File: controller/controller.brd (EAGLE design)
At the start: 100 x 92.7 mm, 26 parts, among them IC1 ATtiny25, IC2 74HC595N

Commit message: Routing erster Versuch
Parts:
- removed JP1: DISABLE, jumper:JP1
- removed R10: (no value), resistor:0617V
- moved SV3 74.0 mm to (76.2, 7.62), turned to 90 degrees
- moved SV2 61.0 mm to (58.4, 7.62), turned to 90 degrees
- moved SV1 51.7 mm to (15.2, 6.35), turned to 0 degrees
- moved R8 41.8 mm to (27.9, 30.5), turned to 0 degrees
- moved R2 39.5 mm to (50.8, 19.1), turned to 270 degrees
- moved R9 37.2 mm to (25.4, 26.7), turned to 0 degrees
- moved LED3 31.4 mm to (55.9, 55.9), turned to 0 degrees
- moved R4 30.6 mm to (50.8, 38.1)
- moved R7 29.0 mm to (30.5, 38.1), turned to 0 degrees
- moved R6 28.4 mm to (33.0, 41.9), turned to 0 degrees
- moved LED4 25.3 mm to (55.9, 47.0), turned to 0 degrees
- moved R3 23.3 mm to (53.3, 30.5)
- moved LED1 21.6 mm to (71.1, 55.9)
- moved LED6 20.5 mm to (25.4, 47.0)
- moved LED5 18.1 mm to (25.4, 55.9)
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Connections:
- removed net N$13: LED6.K, R7.2
- removed net N$14: LED5.K, R6.2
- removed net N$16: LED8.K, R9.2
- removed net N$17: LED7.K, R8.2
- removed net N$4: IC2.13, JP1.1, R10.1
- new net N$11: LED7.A, R8.1
- new net N$12: LED8.A, R9.1
- new net N$5: LED1.A, R2.1
- new net N$8: LED4.A, R5.1
- net GND: now also IC2.13, LED1.K, LED2.K, LED3.K, LED4.K, LED5.K, LED6.K, LED7.K, LED8.K; no longer R10.2, R2.1, R3.1, R4.1, R5.1, R6.1, R7.1, R8.1, R9.1
- net N$10: now also LED6.A, R7.1; no longer LED3.K, R4.2
- net N$6: now also LED2.A, R3.1; no longer LED2.K, R3.2
- net N$7: now also LED3.A, R4.1; no longer LED1.K, R2.2
- net N$9: now also LED5.A, R6.1; no longer LED4.K, R5.2
- net QA: now also R2.2; no longer LED1.A
- net QB: now also R3.2, X1.6; no longer LED2.A, X1.2
- net QC: now also R4.2, X1.2; no longer LED3.A, X1.3
- net QD: now also R5.2; no longer LED4.A, X1.4
- net QE: now also R6.2; no longer LED5.A, X1.6
- net QF: now also R7.2; no longer LED6.A, X1.7
- net QG: now also R8.2; no longer LED7.A, X1.8
- net QH: now also R9.2; no longer LED8.A, X1.9
- net VCC: no longer JP1.2
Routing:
- net VCC: track 315.6 -> 2.54 mm
- net GND: track 286.1 -> 0.00 mm
- net QF: track 130.0 -> 15.2 mm
- net QE: track 115.1 -> 19.0 mm
- net N$5: track 0.00 -> 52.1 mm
- net SCK: track 92.9 -> 47.0 mm
- net MOSI: track 95.9 -> 52.1 mm
- net N$11: track 0.00 -> 35.6 mm
- net QB: track 78.7 -> 45.6 mm
- net N$14: track 29.1 -> 0.00 mm
- net N$12: track 0.00 -> 27.9 mm
- net N$17: track 27.5 -> 0.00 mm
- net RESET: track 29.8 -> 2.54 mm
- net N$4: track 27.3 -> 0.00 mm
- net N$13: track 27.3 -> 0.00 mm
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
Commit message: PLatinenlayout fertig
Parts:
- moved LED4 40.7 mm to (15.2, 49.5), turned to 180 degrees
- moved LED3 40.7 mm to (15.2, 57.1), turned to 180 degrees
- moved SV3 27.4 mm to (50.8, 17.8), turned to 180 degrees
- moved R4 26.9 mm to (24.1, 41.9), turned to 0 degrees
- moved R5 26.9 mm to (21.6, 45.7), turned to 0 degrees
- moved LED6 23.0 mm to (48.3, 49.5)
- moved LED5 22.9 mm to (48.3, 57.1)
- moved LED1 22.6 mm to (53.3, 41.9)
- moved LED2 21.8 mm to (53.3, 34.3)
- moved R3 14.9 mm to (39.4, 35.6)
- moved R2 14.8 mm to (43.2, 31.8), turned to 180 degrees
- moved LED7 14.5 mm to (8.89, 41.9), turned to 180 degrees
- moved LED8 13.3 mm to (8.89, 34.3), turned to 180 degrees
- moved X1 10.2 mm to (30.5, 64.8)
- moved C1 10.2 mm to (36.8, 8.89)
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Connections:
- removed net N$1: SV2.3, SV3.3
- net MISO: now also SV2.3, SV3.3; no longer IC2.14
- net N$2: now also IC2.14; no longer IC2.12
- net N$3: now also IC2.12
- net QB: now also R6.2; no longer R3.2
- net QC: now also R3.2; no longer R4.2
- net QD: now also R7.2, X1.7; no longer R5.2
- net QE: now also R4.2, X1.3; no longer R6.2
- net QF: now also R8.2, X1.8; no longer R7.2
- net QG: now also R5.2, X1.4; no longer R8.2
- net QH: now also X1.9
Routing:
- net VCC: track 2.54 -> 129.7 mm, vias 0 -> 3
- net MISO: track 0.00 -> 55.2 mm
- net N$5: track 52.1 -> 14.5 mm
- net QH: track 3.81 -> 39.7 mm
- net QG: track 7.62 -> 36.6 mm
- net RESET: track 2.54 -> 27.0 mm
- net N$11: track 35.6 -> 12.0 mm
- net QF: track 15.2 -> 38.6 mm
- net N$12: track 27.9 -> 4.86 mm
- net QC: track 15.2 -> 36.6 mm
- net N$6: track 26.7 -> 6.88 mm
- net QD: track 19.0 -> 38.6 mm
- net QE: track 19.0 -> 35.6 mm
- net QA: track 62.3 -> 48.0 mm
- net SCK: track 47.0 -> 59.9 mm
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- added copper zone on layer 16, net GND
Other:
- board size 100 x 92.7 mm -> 63.2 x 71.1 mm

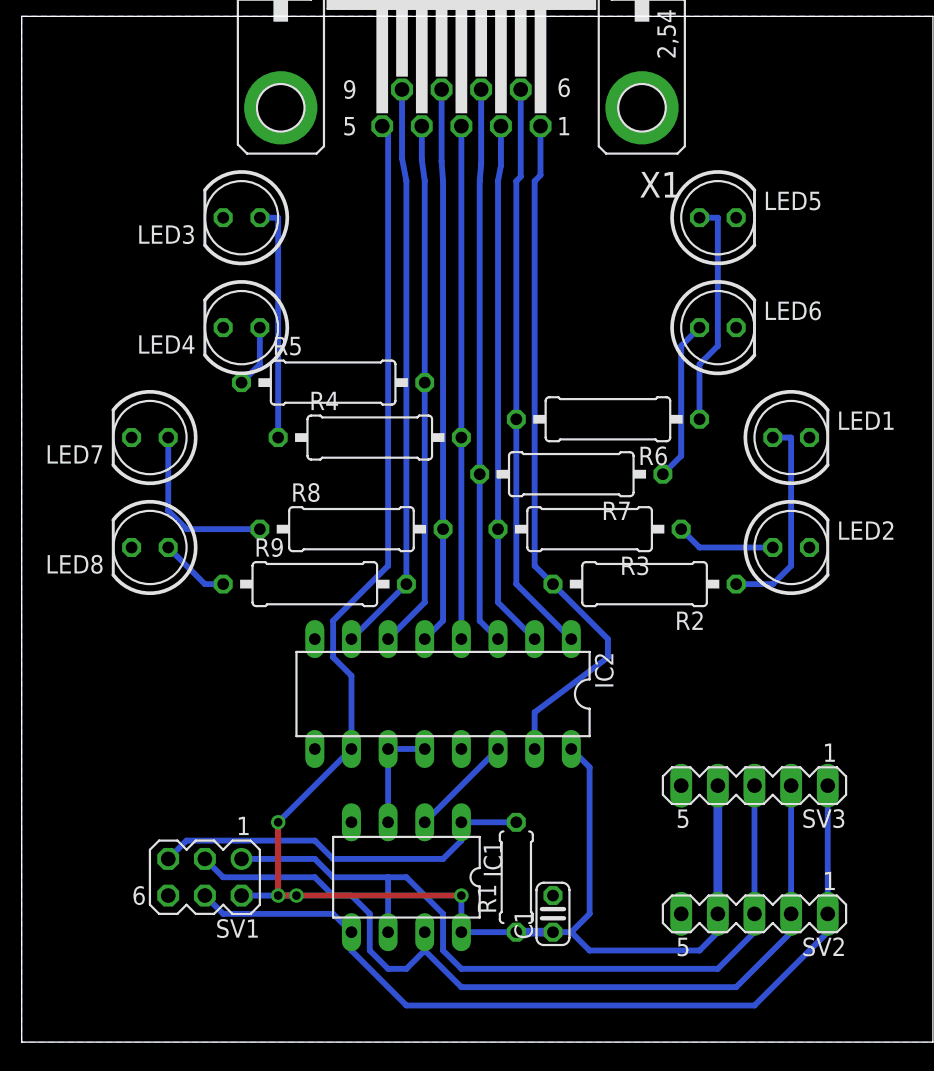
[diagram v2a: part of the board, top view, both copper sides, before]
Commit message: Jumper zum Board hinzugefügt
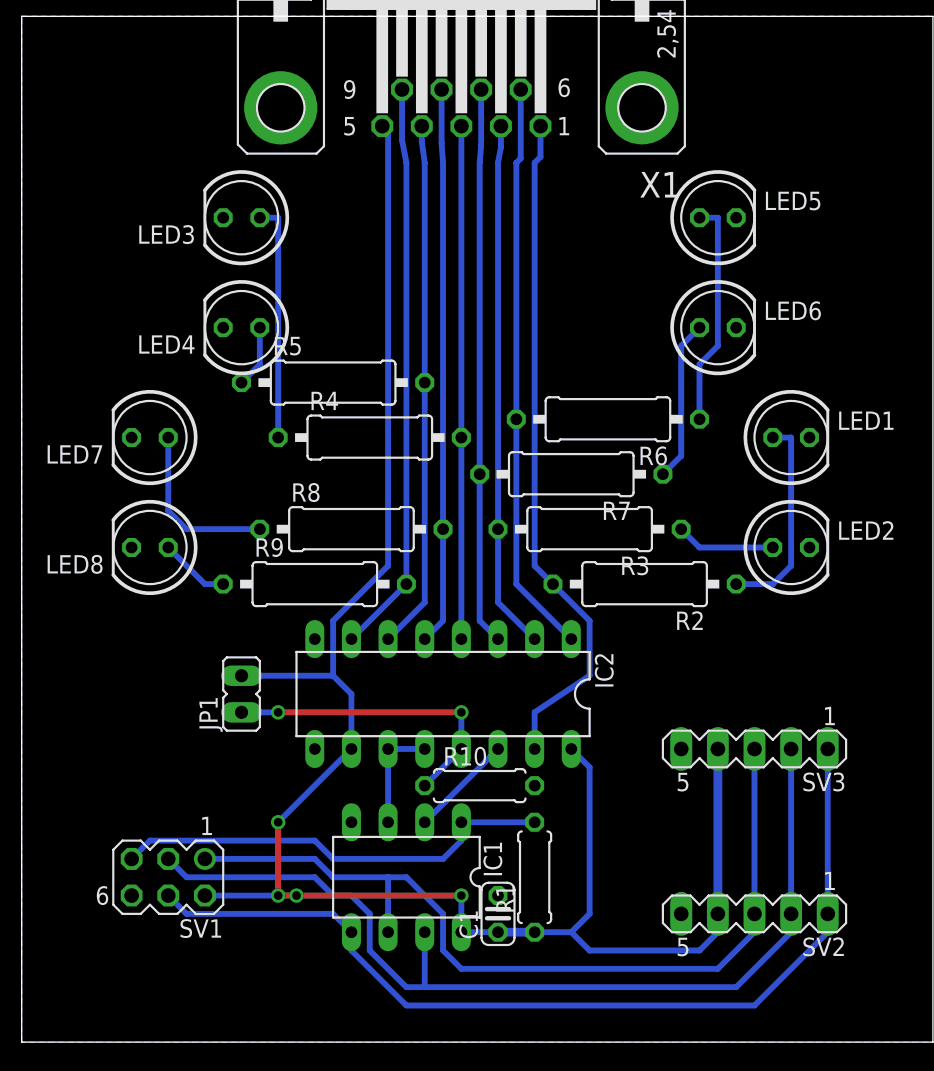
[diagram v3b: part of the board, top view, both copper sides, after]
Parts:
- added JP1: (no value), jumper:JP1
- added R10: 10K, resistor:0207/7
- R2, R3, R4, R5, R6, R7, R8, R9: value (none) -> 1K
- moved C1 3.81 mm to (33.0, 8.89)
- moved SV1 2.54 mm to (10.2, 11.4)
- moved SV3 2.54 mm to (50.8, 20.3)
- moved R1 1.27 mm to (35.6, 11.4)
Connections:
- new net REG_DISABLE: IC2.13, JP1.1, R10.1
- net GND: now also R10.2; no longer IC2.13
- net VCC: now also JP1.2
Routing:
- net REG_DISABLE: track 0.00 -> 21.4 mm, vias 0 -> 2
- net VCC: track 129.7 -> 148.7 mm
- net SCK: track 59.9 -> 66.4 mm
- net MOSI: track 59.3 -> 64.4 mm
- net MISO: track 55.2 -> 60.3 mm
- net RESET: track 27.0 -> 30.8 mm
- net QA: track 48.0 -> 47.0 mm

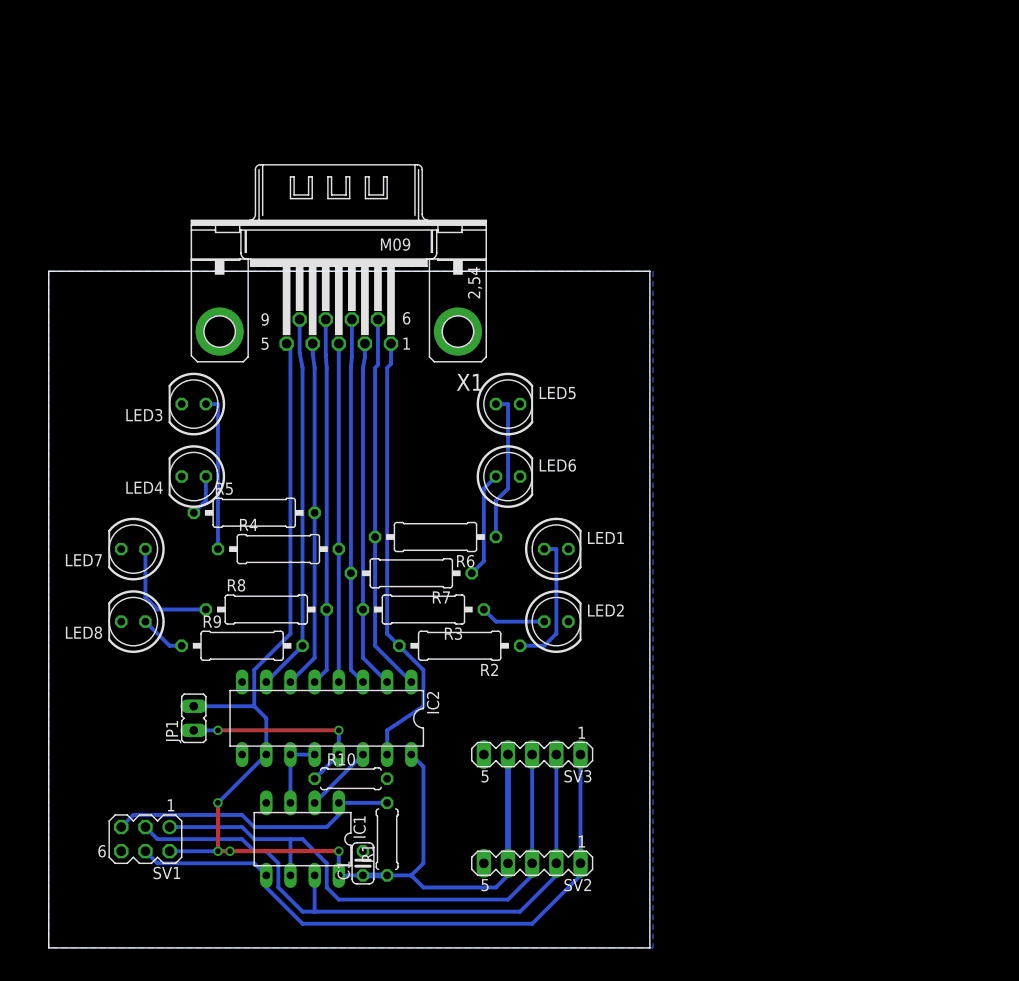
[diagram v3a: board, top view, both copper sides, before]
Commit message: Layout-Tweaks, alle LEDs nun nebeneinander
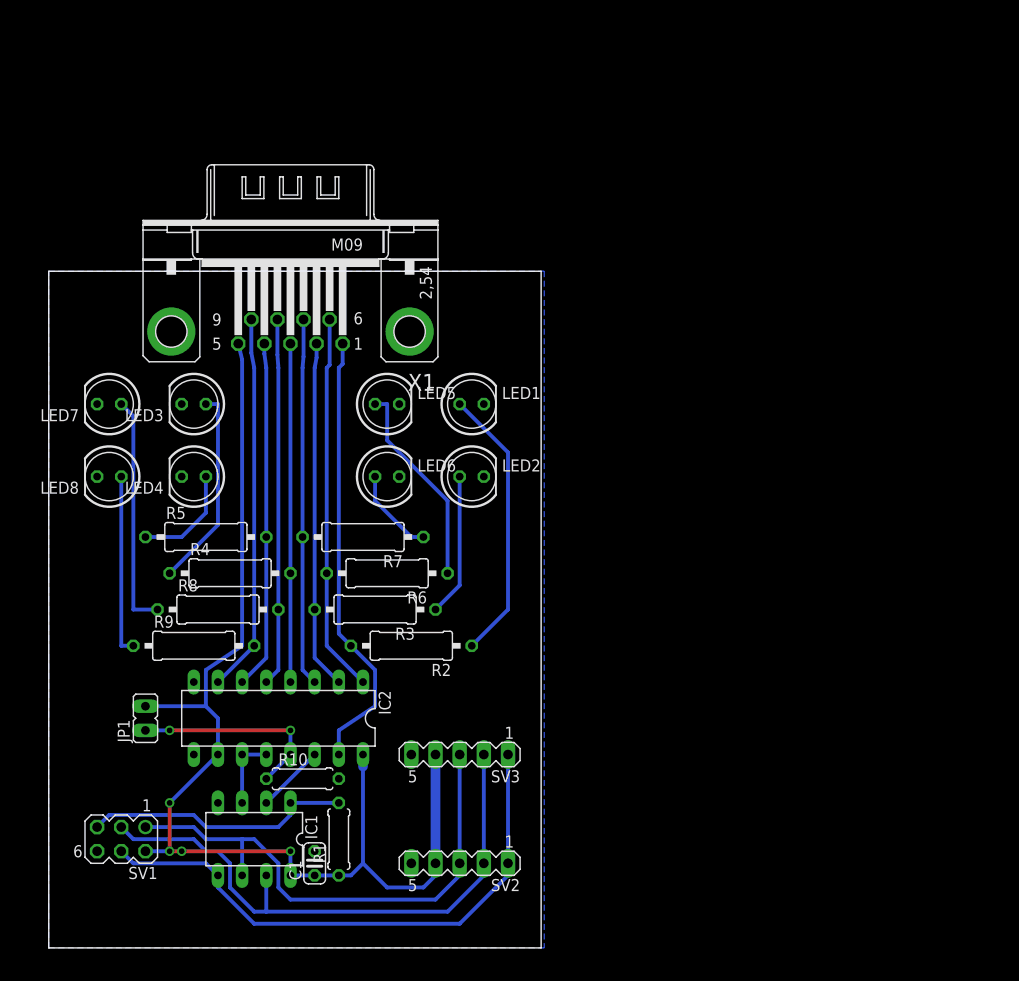
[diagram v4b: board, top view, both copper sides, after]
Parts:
- moved LED1 17.6 mm to (44.5, 57.1)
- moved LED2 17.6 mm to (44.5, 49.5)
- moved LED7 15.5 mm to (6.35, 57.1)
- moved LED8 15.5 mm to (6.35, 49.5)
- moved LED5 12.7 mm to (35.6, 57.1)
- moved LED6 12.7 mm to (35.6, 49.5)
- moved SV2 7.62 mm to (43.2, 8.89)
- moved SV3 7.62 mm to (43.2, 20.3)
- moved R6 6.35 mm to (35.6, 39.4)
- moved R7 6.35 mm to (33.0, 43.2)
- moved R4 5.68 mm to (19.1, 39.4)
- moved R5 5.68 mm to (16.5, 43.2)
- moved C1 5.08 mm to (27.9, 8.89)
- moved IC1 5.08 mm to (21.6, 11.4)
- moved IC2 5.08 mm to (24.1, 24.1)
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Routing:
- net VCC: track 148.7 -> 124.9 mm
- net N$5: track 14.5 -> 29.1 mm
- net N$12: track 4.86 -> 19.1 mm
- net N$11: track 12.0 -> 24.7 mm
- net N$6: track 6.88 -> 15.0 mm
- net N$8: track 4.34 -> 11.2 mm
- net N$9: track 15.8 -> 21.7 mm
- net MISO: track 60.3 -> 55.2 mm
- net MOSI: track 64.4 -> 59.3 mm
- net SCK: track 66.4 -> 61.4 mm
- net N$7: track 16.5 -> 21.2 mm
- net RESET: track 30.8 -> 28.2 mm
- net N$10: track 11.2 -> 9.20 mm
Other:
- board size 63.2 x 71.1 mm -> 51.7 x 71.1 mm
